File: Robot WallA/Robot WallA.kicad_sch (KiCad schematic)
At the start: 4 parts

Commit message: Updated fab files.
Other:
- note added: "Manufacturer: JLCPCB 4 layers 1.6mm outer layer AND inner layer -> 2oz layer stackup -> JLC0416223313 https://jlcpcb.com/impedance https://jlcpcb.com/capabilities/pcb-capabilities"
- note removed: "Manufacturer: JLCPCB 4 layers 1.6mm 2oz outer layer 0.5oz inner layer https://jlcpcb.com/impedance https://jlcpcb.com/capabilities/pcb-capabilities"
- company: (none) -> Socotec Monitoring
- title: (none) -> Robot Wall-A
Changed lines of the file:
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@@
 	(generator_version "9.0")
 	(paper "A4")
+	(title_block
+		(title "Robot Wall-A")
+		(date "2025-09-20")
+		(rev "v1.0")
+		(company "Socotec Monitoring")
+		(comment 1 "GDU")
+		(comment 2 "THO")
+	)
 	(text "5V_DEBUG est pour alimenter UNIQUEMENT le UC"
 		(exclude_from_sim no)
@@
 		)
 	)
-	(text "Manufacturer:\nJLCPCB\n4 layers\n1.6mm\n2oz outer layer\n0.5oz inner layer\nhttps://jlcpcb.com/impedance\nhttps://jlcpcb.com/capabilities/pcb-capabilities"
+	(text "Manufacturer:\nJLCPCB\n4 layers\n1.6mm\nouter layer AND inner layer -> 2oz\nlayer stackup -> JLC0416223313\nhttps://jlcpcb.com/impedance\nhttps://jlcpcb.com/capabilities/pcb-capabilities"
 		(exclude_from_sim no)
 		(at 116.84 177.292 0)
@@
 			)
 		)
+		(property "MPN" ""
+			(at 27.94 180.34 90)
+			(effects
+				(font
+					(size 1.27 1.27)
+				)
+				(hide yes)
+			)
+		)
 		(pin "1"
 		)
@@
 			)
 		)
+		(property "MPN" ""
+			(at 27.94 190.5 90)
+			(effects
+				(font
+					(size 1.27 1.27)
+				)
+				(hide yes)
+			)
+		)
 		(pin "1"
 		)
@@
 			)
 		)
+		(property "MPN" ""
+			(at 52.07 180.34 90)
+			(effects
+				(font
+					(size 1.27 1.27)
+				)
+				(hide yes)
+			)
+		)
 		(pin "1"
 		)
@@
 			(effects
 				(font
+					(size 1.27 1.27)
+				)
+				(hide yes)
+			)
+		)
+		(property "MPN" ""
+			(at 52.07 190.5 90)
+			(effects
+				(font

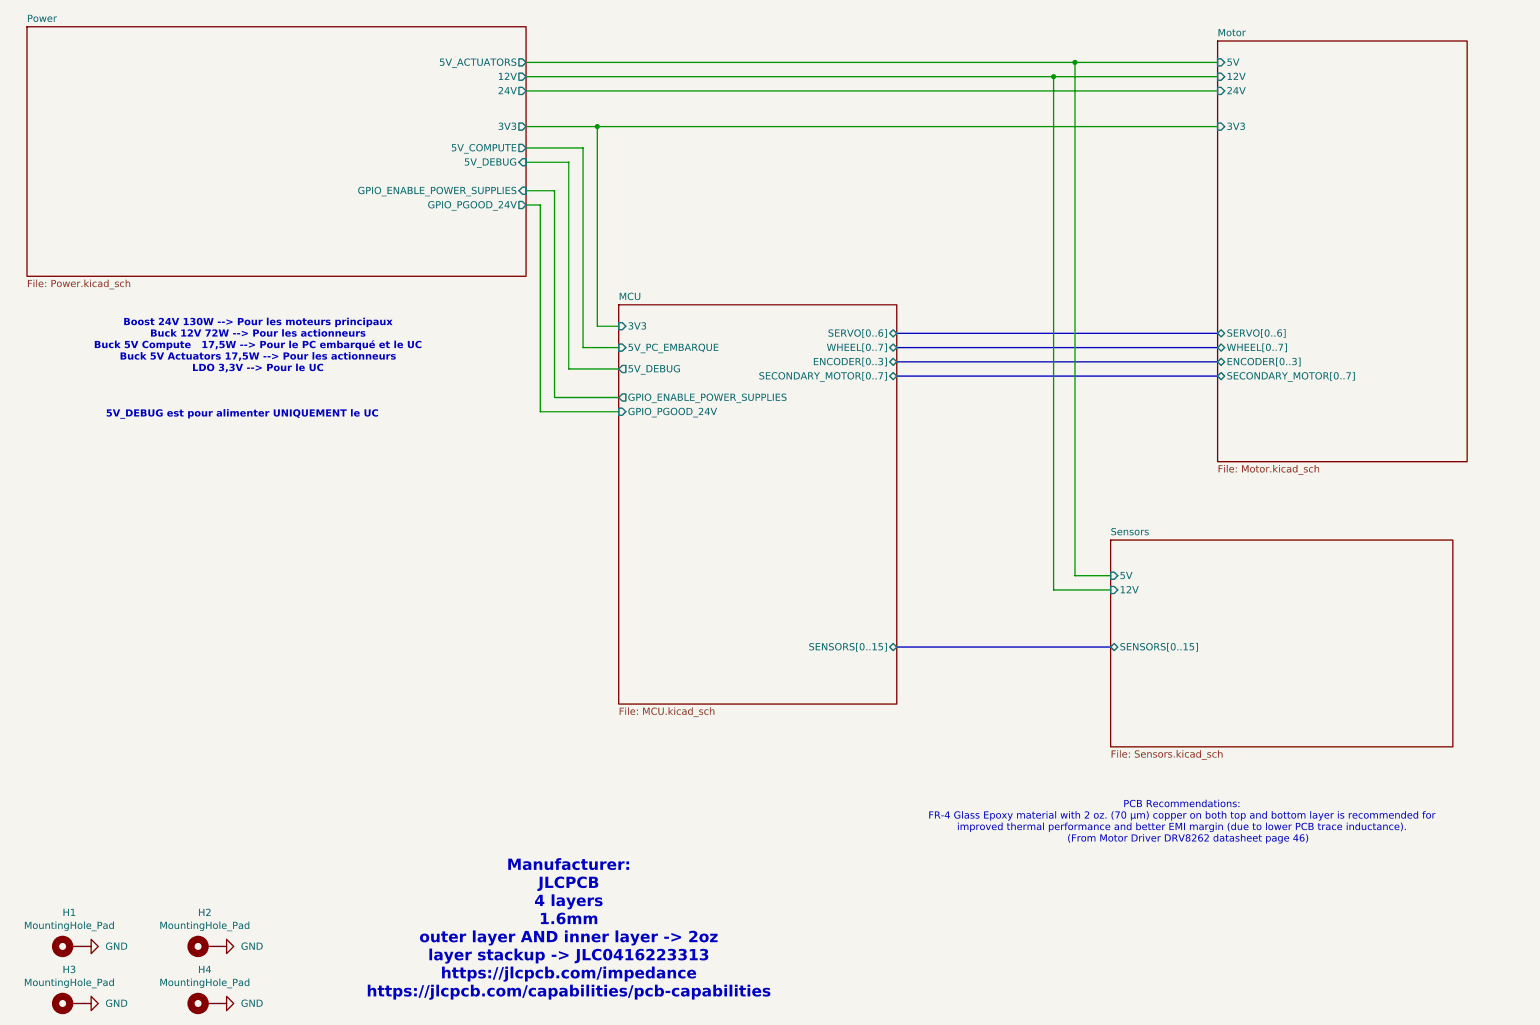
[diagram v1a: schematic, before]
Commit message: Added diode for Type-C connector in case we accidentally power the board with this connector.
Updated fab files
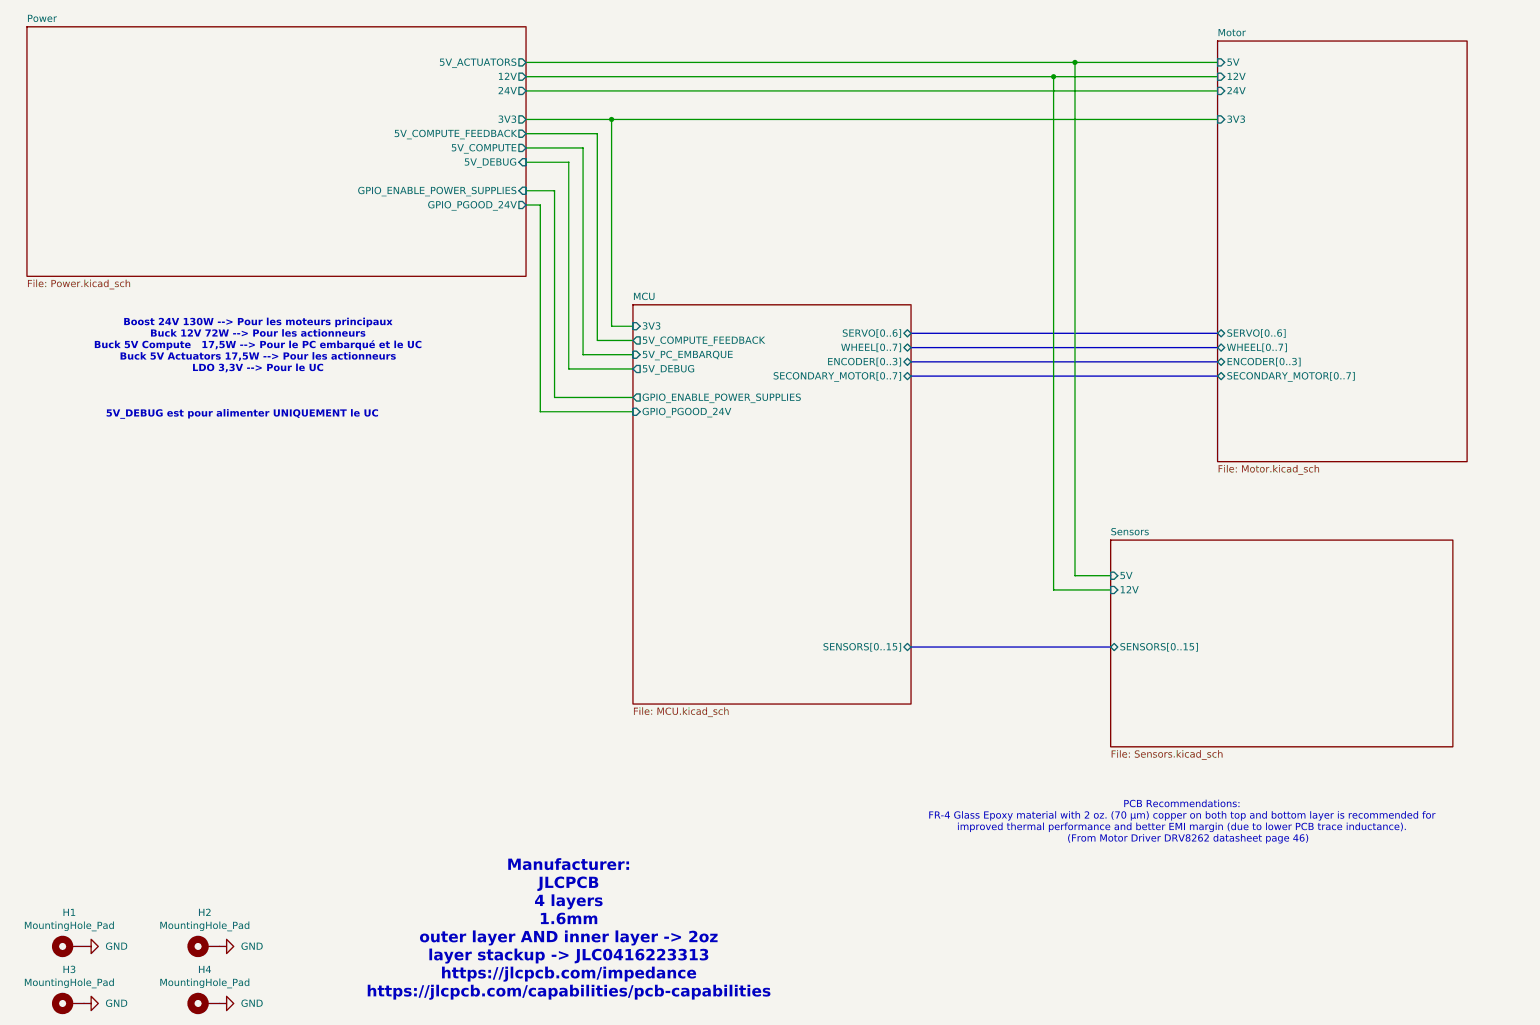
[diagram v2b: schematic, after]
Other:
- sheet MCU ports: added 5V_COMPUTE_FEEDBACK; removed none
- sheet Power ports: added 5V_COMPUTE_FEEDBACK; removed none
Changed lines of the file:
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@@
 	)
 	(junction
-		(at 121.92 34.29)
+		(at 124.46 33.02)
 		(diameter 0)
 		(color 0 0 0 0)
@@
 	(wire
 		(pts
-			(xy 121.92 69.85) (xy 125.73 69.85)
+			(xy 124.46 69.85) (xy 128.27 69.85)
 		)
 		(stroke
@@
 	(bus
 		(pts
-			(xy 175.26 76.2) (xy 232.41 76.2)
+			(xy 177.8 76.2) (xy 232.41 76.2)
 		)
 		(stroke
@@
 	(wire
 		(pts
-			(xy 109.22 34.29) (xy 121.92 34.29)
+			(xy 121.92 72.39) (xy 128.27 72.39)
+		)
+		(stroke
+			(width 0)
+			(type default)
+		)
+	)
+	(wire
+		(pts
+			(xy 109.22 33.02) (xy 124.46 33.02)
 		)
 		(stroke
@@
 	(wire
 		(pts
-			(xy 125.73 82.55) (xy 114.3 82.55)
+			(xy 128.27 82.55) (xy 114.3 82.55)
 		)
 		(stroke
@@
 	(bus
 		(pts
-			(xy 175.26 71.12) (xy 232.41 71.12)
+			(xy 177.8 71.12) (xy 232.41 71.12)
 		)
 		(stroke
@@
 	(bus
 		(pts
-			(xy 175.26 73.66) (xy 232.41 73.66)
+			(xy 177.8 73.66) (xy 232.41 73.66)
 		)
 		(stroke
@@
 		)
 	)
+	(wire
+		(pts
+			(xy 124.46 33.02) (xy 124.46 69.85)
+		)
+		(stroke
+			(width 0)
+			(type default)
+		)
+	)
+	(wire
+		(pts
+			(xy 109.22 35.56) (xy 121.92 35.56)
+		)
+		(stroke
+			(width 0)
+			(type default)
+		)
+	)
 	(bus
 		(pts
-			(xy 175.26 127) (xy 213.36 127)
-		)
-		(stroke
-			(width 0)
-			(type default)
-		)
-	)
-	(wire
-		(pts
-			(xy 121.92 34.29) (xy 232.41 34.29)
-		)
-		(stroke
-			(width 0)
-			(type default)
-		)
-	)
-	(wire
-		(pts
-			(xy 111.76 85.09) (xy 125.73 85.09)
+			(xy 177.8 127) (xy 213.36 127)
+		)
+		(stroke
+			(width 0)
+			(type default)
+		)
+	)
+	(wire
+		(pts
+			(xy 111.76 85.09) (xy 128.27 85.09)
 		)
 		(stroke
@@
 	(wire
 		(pts
-			(xy 119.38 73.66) (xy 125.73 73.66)
-		)
-		(stroke
-			(width 0)
-			(type default)
-		)
-	)
-	(wire
-		(pts
-			(xy 121.92 34.29) (xy 121.92 69.85)
-		)
-		(stroke
-			(width 0)
-			(type default)
-		)
-	)
-	(wire
-		(pts
-			(xy 119.38 38.1) (xy 119.38 73.66)
+			(xy 119.38 74.93) (xy 128.27 74.93)
+		)
+		(stroke
+			(width 0)
+			(type default)
+		)
+	)
+	(wire
+		(pts
+			(xy 119.38 38.1) (xy 119.38 74.93)
+		)
+		(stroke
+			(width 0)
+			(type default)
+		)
+	)
+	(wire
+		(pts
+			(xy 121.92 35.56) (xy 121.92 72.39)
 		)
 		(stroke
@@
 	(bus
 		(pts
-			(xy 175.26 78.74) (xy 232.41 78.74)
+			(xy 177.8 78.74) (xy 232.41 78.74)
 		)
 		(stroke
@@
 	(wire
 		(pts
-			(xy 125.73 77.47) (xy 116.84 77.47)
+			(xy 124.46 33.02) (xy 232.41 33.02)
+		)
+		(stroke
+			(width 0)
+			(type default)
+		)
+	)
+	(wire
+		(pts
+			(xy 128.27 77.47) (xy 116.84 77.47)
 		)
 		(stroke
@@
 		)
 		(pin "3V3" input
-			(at 232.41 34.29 180)
+			(at 232.41 33.02 180)
 			(effects
 				(font
@@
 	)
 	(sheet
-		(at 125.73 66.04)
+		(at 128.27 66.04)
 		(size 49.53 71.12)
 		(exclude_from_sim no)
@@
 		)
 		(property "Sheetname" "MCU"
-			(at 125.73 65.3284 0)
+			(at 128.27 65.3284 0)
 			(effects
 				(font
@@
 		)
 		(property "Sheetfile" "MCU.kicad_sch"
-			(at 125.73 137.7446 0)
+			(at 128.27 137.7446 0)
 			(effects
 				(font
@@
 		)
 		(pin "3V3" input
-			(at 125.73 69.85 180)
+			(at 128.27 69.85 180)
 			(effects
 				(font
@@
 		)
 		(pin "5V_PC_EMBARQUE" input
-			(at 125.73 73.66 180)
+			(at 128.27 74.93 180)
 			(effects
 				(font
@@
 		)
 		(pin "5V_DEBUG" output
-			(at 125.73 77.47 180)
+			(at 128.27 77.47 180)
 			(effects
 				(font
@@
 		)
 		(pin "SERVO[0..6]" bidirectional
-			(at 175.26 71.12 0)
+			(at 177.8 71.12 0)
 			(effects
 				(font
@@
 		)
 		(pin "WHEEL[0..7]" bidirectional
-			(at 175.26 73.66 0)
+			(at 177.8 73.66 0)
 			(effects
 				(font
@@
 		)
 		(pin "ENCODER[0..3]" bidirectional
-			(at 175.26 76.2 0)
+			(at 177.8 76.2 0)
 			(effects
 				(font
@@
 		)
 		(pin "GPIO_ENABLE_POWER_SUPPLIES" output
-			(at 125.73 82.55 180)
+			(at 128.27 82.55 180)
 			(effects
 				(font
@@
 		)
 		(pin "GPIO_PGOOD_24V" input
-			(at 125.73 85.09 180)
+			(at 128.27 85.09 180)
 			(effects
 				(font
@@
 		)
 		(pin "SECONDARY_MOTOR[0..7]" bidirectional
-			(at 175.26 78.74 0)
+			(at 177.8 78.74 0)
 			(effects
 				(font
@@
 		)
 		(pin "SENSORS[0..15]" bidirectional
-			(at 175.26 127 0)
-			(effects
-				(font
-					(size 1.27 1.27)
-				)
-				(justify right)
+			(at 177.8 127 0)
+			(effects
+				(font
+					(size 1.27 1.27)
+				)
+				(justify right)
+			)
+		)
+		(pin "5V_COMPUTE_FEEDBACK" output
+			(at 128.27 72.39 180)
+			(effects
+				(font
+					(size 1.27 1.27)
+				)
+				(justify left)
 			)
 		)
@@
 		)
 		(pin "3V3" output
-			(at 109.22 34.29 0)
+			(at 109.22 33.02 0)
 			(effects
 				(font
@@
 			(effects
 				(font
+					(size 1.27 1.27)
+				)
+				(justify right)
+			)
+		)
+		(pin "5V_COMPUTE_FEEDBACK" output
+			(at 109.22 35.56 0)
+			(effects
+				(font
